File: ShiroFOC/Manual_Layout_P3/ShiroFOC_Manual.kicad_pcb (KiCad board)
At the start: 6 copper layers, 45 x 45 mm, 329 parts, among them J1 Motor phases - solder wires, J1001 TC2030-NL SWD, J101 DC input - solder wires, J201 USB-C service, J501 BRAKE RESISTOR, J502 5V PWM FAN, J601 EXT ENCODER / HALL, J801 CAN 1, J802 CAN 2, Q201 CSD17483F4, Q301 CSD17483F4, Q501 ISZ080N10NM6 100V, Q801 CSD17483F4, Q802 CSD87502Q2, SW301 RESET, U1 CSD88599Q5DC, U2 CSD88599Q5DC, U201 LMR36510FADDAR, U202 USBLC6-2SC6, U203 TPS2121RUXR, U204 TLV75533PDYDR, U205 MPM3620AGQV-Z, U3 CSD88599Q5DC, U4 STSPIN32G4, U501 UCC27517ADBVR, U502 TLV3012BIDCKR, U503 74AHCT1G125W5-7, U601 AS5047P-ATSM, U602 TMUX1574PW, U603 74LVC3G17, U604 TPS2553DBVR, U701 BMI323, U801 TCAN3413DRBR, U901 CP2102N-A02-GQFN20, Y301 24MHz 7pF

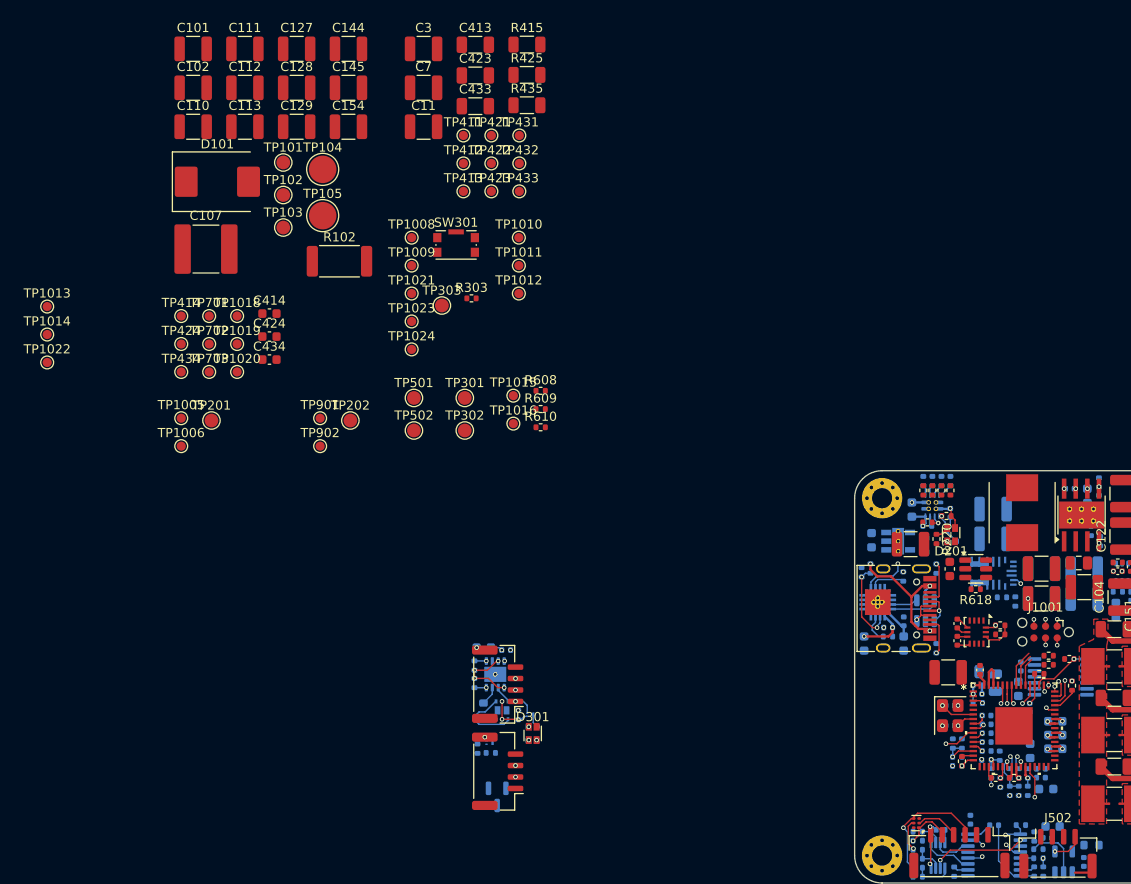
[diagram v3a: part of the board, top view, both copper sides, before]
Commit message: opamp circuits revised
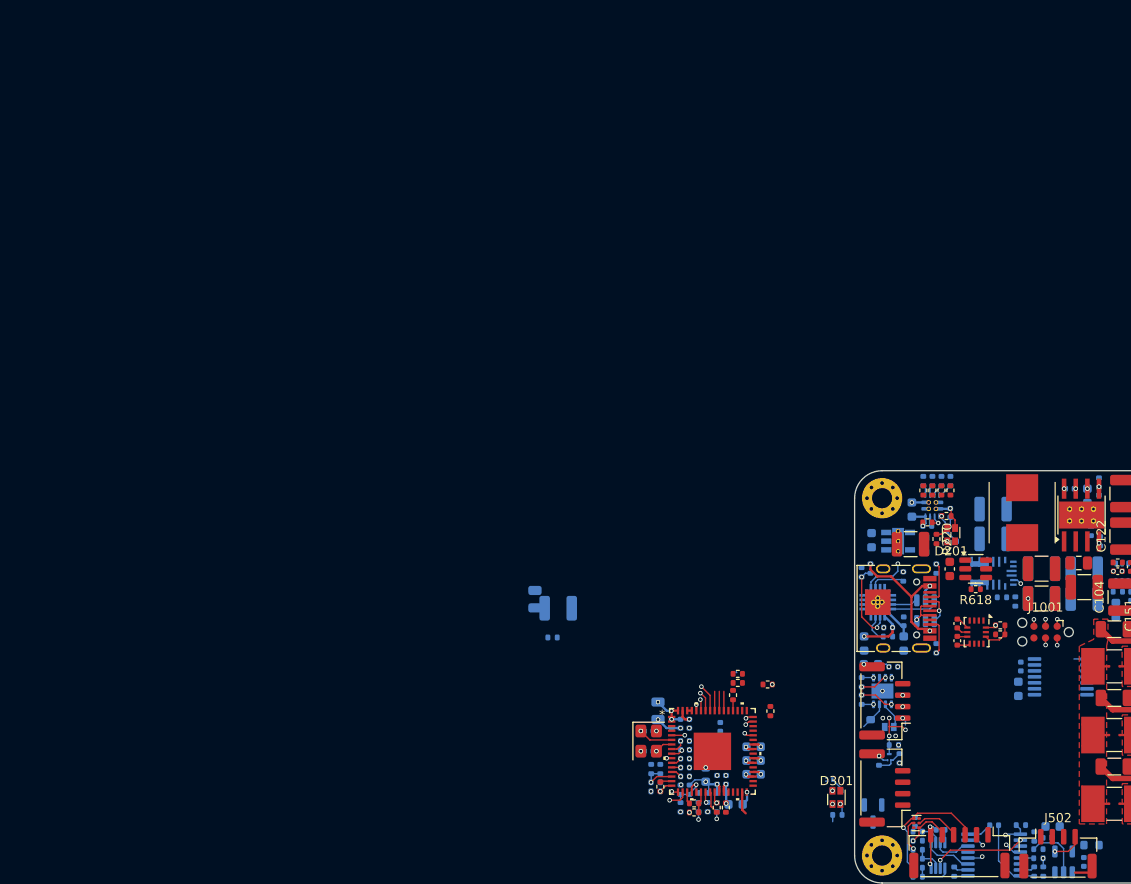
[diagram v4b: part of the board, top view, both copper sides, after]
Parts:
- removed C101, C102, C110, C111, C112, C113, C127, C128, C129, C144, C145, C154: 10uF, Capacitor_SMD:C_1210_3225Metric
- removed C107: RC DAMP C - TUNE, Capacitor_SMD:C_2220_5750Metric
- removed C11, C3, C7: 4.7uF, Capacitor_SMD:C_1210_3225Metric
- removed C413, C423, C433: TUNE DNP, Capacitor_SMD:C_1206_3216Metric
- removed C414, C424, C434: 47pF C0G, Capacitor_SMD:C_0603_1608Metric
- removed D101: VM TVS - SELECT AFTER TEST, Diode_SMD:D_SMC
- removed R102: RC DAMP R - TUNE, Resistor_SMD:R_2512_6332Metric
- removed R303: 2k2, Resistor_SMD:R_0402_1005Metric
- removed R415, R425, R435: TUNE DNP, Resistor_SMD:R_1206_3216Metric
- removed R608, R609, R610: 4.7k DNP, Resistor_SMD:R_0402_1005Metric
- removed SW301: RESET, Button_Switch_SMD:SW_Push_1P1T-SH_NO_CK_KMR2xxG
- removed TP1005: 5V_SYS, TestPoint:TestPoint_Pad_D1.0mm
- removed TP1006: 3V3, TestPoint:TestPoint_Pad_D1.0mm
- removed TP1008: SWDIO, TestPoint:TestPoint_Pad_D1.0mm
- removed TP1009: SWCLK, TestPoint:TestPoint_Pad_D1.0mm
- removed TP101: VM, TestPoint:TestPoint_Pad_D1.5mm
- removed TP1010: ENC_SPI_CLK, TestPoint:TestPoint_Pad_D1.0mm
- removed TP1011: SPI3_MISO, TestPoint:TestPoint_Pad_D1.0mm
- removed TP1012: ENC_SPI_MOSI, TestPoint:TestPoint_Pad_D1.0mm
- removed TP1013: FDCAN1_TX, TestPoint:TestPoint_Pad_D1.0mm
- removed TP1014: FDCAN1_RX, TestPoint:TestPoint_Pad_D1.0mm
- removed TP1015: FEEDBACK_A_H1, TestPoint:TestPoint_Pad_D1.0mm
- removed TP1016: FEEDBACK_B_H2, TestPoint:TestPoint_Pad_D1.0mm
- removed TP1018: OPO_U1, TestPoint:TestPoint_Pad_D1.0mm
- removed TP1019: OPO_V1, TestPoint:TestPoint_Pad_D1.0mm
- removed TP102: GND, TestPoint:TestPoint_Pad_D1.5mm
- removed TP1020: OPO_W1, TestPoint:TestPoint_Pad_D1.0mm
- removed TP1021: CAN_TERM_DISABLE, TestPoint:TestPoint_Pad_D1.0mm
- removed TP1022: CAN_STB, TestPoint:TestPoint_Pad_D1.0mm
- removed TP1023: EXT_POWER_FAULT_N, TestPoint:TestPoint_Pad_D1.0mm
- removed TP1024: I2C2_SDA, TestPoint:TestPoint_Pad_D1.0mm
- removed TP103: VBUS_SENSE, TestPoint:TestPoint_Pad_D1.5mm
- removed TP104: VM BULK, TestPoint:TestPoint_Pad_D3.0mm
- removed TP105: GND BULK, TestPoint:TestPoint_Pad_D3.0mm
- removed TP201: PWR_SOURCE_STATUS, TestPoint:TestPoint_Pad_D1.5mm
- removed TP202: 5V_USB, TestPoint:TestPoint_Pad_D1.5mm
- removed TP301: VCC, TestPoint:TestPoint_Pad_D1.5mm
- removed TP302: SCREF, TestPoint:TestPoint_Pad_D1.5mm
- removed TP303: NRST, TestPoint:TestPoint_Pad_D1.5mm
- removed TP411, TP421, TP431: GL, TestPoint:TestPoint_Pad_D1.0mm
- removed TP412, TP422, TP432: SOURCE, TestPoint:TestPoint_Pad_D1.0mm
- removed TP413, TP423, TP433: PHASE, TestPoint:TestPoint_Pad_D1.0mm
- removed TP414, TP424, TP434: SCOPE GND, TestPoint:TestPoint_Pad_D1.0mm
- removed TP501: BRAKE_GATE, TestPoint:TestPoint_Pad_D1.5mm
- removed TP502: BRAKE_SWITCH, TestPoint:TestPoint_Pad_D1.5mm
- removed TP701: NTC_PHASE_A, TestPoint:TestPoint_Pad_D1.0mm
- removed TP702: NTC_PHASE_B, TestPoint:TestPoint_Pad_D1.0mm
- removed TP703: NTC_PHASE_C, TestPoint:TestPoint_Pad_D1.0mm
- removed TP901: USB_UART_TX, TestPoint:TestPoint_Pad_D1.0mm
- removed TP902: USB_UART_RX, TestPoint:TestPoint_Pad_D1.0mm
- C312, C313: moved to B.Cu
- R301, R428: moved to F.Cu
- moved C311 51.1 mm to (-57.4, -8.48)
- moved R604 47.0 mm to (-55.5, -4.30)
- moved R803 44.6 mm to (-17.6, 8.89), turned to 90 degrees
- moved R804 43.8 mm to (-19.8, 9.14)
- moved Q801 43.6 mm to (-18.7, 8.76), turned to 90 degrees
- moved C312 43.1 mm to (-54.9, -7.49), turned to 0 degrees
- moved C801 42.3 mm to (-18.3, -1.10)
- moved C802 42.3 mm to (-20.7, -1.37)
- moved J801 42.3 mm to (-19.2, 2.62)
- moved J802 42.3 mm to (-19.2, 12.1)
- moved Q802 42.3 mm to (-18.7, 5.47)
- moved R801 42.3 mm to (-21.7, 2.50)
- moved R805 42.3 mm to (-21.7, 0.59)
- moved R802 42.3 mm to (-20.8, 5.50)
- moved U801 42.3 mm to (-19.5, 1.55)
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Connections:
- J801 pad 4: /CAN interface/CAN_SHIELD -> GND
- J802 pad 4: /CAN interface/CAN_SHIELD -> GND
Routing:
- net /MCU / clock / SWD/SWDIO: track 9.69 -> 1.69 mm, vias 2 -> 1
- net VREF+: track 0.55 -> 6.71 mm, vias 3 -> 2
- net CAN_TERM_DISABLE: track 0.00 -> 5.43 mm, vias 0 -> 2
- net AS5047P_CS_N: track 6.60 -> 1.42 mm
- net GND: track 62.8 -> 67.7 mm, vias 15 -> 27
- net Net-(Q802A-S1): track 7.38 -> 2.63 mm, vias 0 -> 2
- net /CAN interface/CANH_BUS: track 12.0 -> 7.40 mm, vias 2 -> 1
- net USB_UART_RX: track 10.6 -> 6.62 mm, vias 2 -> 1
- net /CAN interface/CANL_BUS: track 12.1 -> 8.27 mm, vias 2 -> 1
- net CAN_STB: track 4.84 -> 1.30 mm, vias 2 -> 1
- net /Current / temperature/OPP_W1: track 4.59 -> 1.16 mm
- net VM: track 57.4 -> 54.2 mm
- net Net-(Q801-G): track 0.00 -> 3.00 mm
- net FAN_PWM: track 3.48 -> 0.55 mm
- net USB_UART_TX: track 2.75 -> 0.00 mm
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
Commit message: weekend progress
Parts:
- added C101: 10uF, Capacitor_SMD:C_1210_3225Metric, F.Cu at (39.1, -26.7)
- added C102: 10uF, Capacitor_SMD:C_1210_3225Metric, F.Cu at (39.1, -22.4)
- added C11: 4.7uF, Capacitor_SMD:C_1210_3225Metric, F.Cu at (64.2, -18.2)
- added C110: 10uF, Capacitor_SMD:C_1210_3225Metric, F.Cu at (39.1, -18.2)
- added C111: 10uF, Capacitor_SMD:C_1210_3225Metric, F.Cu at (44.7, -26.7)
- added C112: 10uF, Capacitor_SMD:C_1210_3225Metric, F.Cu at (44.7, -22.4)
- added C113: 10uF, Capacitor_SMD:C_1210_3225Metric, F.Cu at (44.7, -18.2)
- added C127: 10uF, Capacitor_SMD:C_1210_3225Metric, F.Cu at (50.4, -26.7)
- added C128: 10uF, Capacitor_SMD:C_1210_3225Metric, F.Cu at (50.4, -22.4)
- added C129: 10uF, Capacitor_SMD:C_1210_3225Metric, F.Cu at (50.4, -18.2)
- added C144: 10uF, Capacitor_SMD:C_1210_3225Metric, F.Cu at (56.0, -26.7)
- added C145: 10uF, Capacitor_SMD:C_1210_3225Metric, F.Cu at (56.0, -22.4)
- added C154: 10uF, Capacitor_SMD:C_1210_3225Metric, F.Cu at (56.0, -18.2)
- added C3: 4.7uF, Capacitor_SMD:C_1210_3225Metric, F.Cu at (64.2, -26.7)
- added C7: 4.7uF, Capacitor_SMD:C_1210_3225Metric, F.Cu at (64.2, -22.4)
- added R303: 2k2, Resistor_SMD:R_0402_1005Metric, B.Cu at (-13.3, 3.29)
- C311, C601, C602, C607, R315: moved to F.Cu
- J1: footprint ShiroFOCLib:WireSolder_Phase_1x03_P6.35mm_D2.90mm_Pad4.10mm -> ShiroFOCLib:WireSolder_Phase_1x03_P6.35mm_D3.00mm_Pad5.00x4.10mm_4xD0.40mm
- J101: footprint ShiroFOCLib:WireSolder_DC_1x02_P6.35mm_D2.70mm_Pad4.10mm -> ShiroFOCLib:WireSolder_DC_1x02_P6.35mm_D3.00mm_Pad5.00x4.10mm_4xD0.40mm
- J601: footprint Connector_JST:JST_GH_BM06B-GHS-TBT_1x06-1MP_P1.25mm_Vertical -> Connector_JST:JST_GH_SM06B-GHS-TB_1x06-1MP_P1.25mm_Horizontal
- J801, J802: footprint Connector_JST:JST_GH_BM04B-GHS-TBT_1x04-1MP_P1.25mm_Vertical -> Connector_JST:JST_GH_SM03B-GHS-TB_1x03-1MP_P1.25mm_Horizontal
- R309, R903, TH701, TH702, TH703: moved to B.Cu
- moved C118 68.8 mm to (10.8, 28.7), turned to 180 degrees
- moved C119 63.3 mm to (15.4, 28.8)
- moved C312 50.5 mm to (-6.23, 6.09), turned to -90 degrees
- moved C311 48.9 mm to (-9.55, 1.54), turned to 180 degrees
- moved TH701 44.3 mm to (10.3, -0.64)
- moved TH703 44.3 mm to (10.3, 14.3)
- moved TH702 42.4 mm to (10.3, 6.85)
- moved R604 41.9 mm to (-14.2, 3.29), turned to -90 degrees
- moved R103 35.3 mm to (-26.6, -0.18)
- moved R105 34.9 mm to (-29.6, 0.02)
- moved C314 33.5 mm to (-3.70, 4.70)
- moved R106 32.8 mm to (-28.6, 0.02), turned to -90 degrees
- moved R903 32.7 mm to (0.91, 5.88), turned to 0 degrees
- moved R311 32.7 mm to (-2.58, 0.56), turned to 90 degrees
- moved C607 32.5 mm to (-9.28, -14.0)
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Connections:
- C711 pad 1: NTC_PHASE_A -> NTC_PHASE_B
- C712 pad 1: NTC_PHASE_B -> NTC_PHASE_A
- R701 pad 2: /Current / temperature/NTC_A_RAW -> /Current / temperature/NTC_B_RAW
- R702 pad 2: /Current / temperature/NTC_B_RAW -> /Current / temperature/NTC_A_RAW
- R711 pad 1: /Current / temperature/NTC_A_RAW -> /Current / temperature/NTC_B_RAW
- R711 pad 2: NTC_PHASE_A -> NTC_PHASE_B
- R712 pad 1: /Current / temperature/NTC_B_RAW -> /Current / temperature/NTC_A_RAW
- R712 pad 2: NTC_PHASE_B -> NTC_PHASE_A
- TH701 pad 1: /Current / temperature/NTC_A_RAW -> /Current / temperature/NTC_B_RAW
- TH702 pad 1: /Current / temperature/NTC_B_RAW -> /Current / temperature/NTC_A_RAW
- U4 pad 11: NTC_PHASE_B -> NTC_PHASE_A
- U4 pad 12: NTC_PHASE_A -> NTC_PHASE_B
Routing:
- net CAN_TERM_DISABLE: track 5.43 -> 23.4 mm
- net I2C2_SCL: track 0.00 -> 17.0 mm, vias 0 -> 2
- net /CAN interface/CANL_BUS: track 8.27 -> 24.4 mm
- net FDCAN1_RX: track 4.42 -> 18.3 mm
- net I2C2_SDA: track 2.17 -> 15.5 mm
- net 3V3: track 40.0 -> 28.7 mm, vias 11 -> 15
- net FDCAN1_TX: track 7.24 -> 18.2 mm
- net /MCU / clock / SWD/NRST: track 2.40 -> 12.5 mm
- net /CAN interface/CANH_BUS: track 7.40 -> 17.2 mm
- net CAN_STB: track 1.30 -> 9.92 mm, vias 1 -> 2
- net SPI3_SCK_MCU: track 2.10 -> 10.1 mm, vias 0 -> 1
- net SPI3_MISO: track 2.10 -> 9.19 mm, vias 0 -> 1
- net VBUS_SENSE: track 3.13 -> 9.49 mm
- net AS5047P_CS_N: track 1.42 -> 7.77 mm
- net SPI3_MOSI_MCU: track 2.10 -> 8.22 mm, vias 0 -> 1
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
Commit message: half bridge progress
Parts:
- J1: footprint ShiroFOCLib:WireSolder_Phase_1x03_P6.35mm_D3.00mm_Pad5.00x4.10mm_4xD0.40mm -> ShiroFOCLib:WireSolder_Phase_1x03_P6.85mm_D3.00mm_Pad5.00x4.10mm_4xD0.40mm
- J101: footprint ShiroFOCLib:WireSolder_DC_1x02_P6.35mm_D3.00mm_Pad5.00x4.10mm_4xD0.40mm -> ShiroFOCLib:WireSolder_DC_1x02_P6.85mm_D3.00mm_Pad5.00x4.10mm_4xD0.40mm
- moved R607 9.66 mm to (-21.9, 12.6)
- moved C603 9.66 mm to (-16.4, 3.21)
- moved C604 9.66 mm to (-16.6, 12.6)
- moved C605 9.66 mm to (-21.5, 8.72)
- moved D601 9.66 mm to (-16.6, 12.6)
- moved J601 9.66 mm to (-19.3, 5.67)
- moved R103 9.66 mm to (-17.0, -0.80)
- moved R105 9.66 mm to (-20.0, -0.60)
- moved R106 9.66 mm to (-19.0, -0.60)
- moved R305 9.66 mm to (-16.4, 1.32)
- moved R306 9.66 mm to (-17.5, 8.62)
- moved R307 9.66 mm to (-21.5, -0.14)
- moved R605 9.66 mm to (-20.9, 12.6)
- moved R606 9.66 mm to (-18.9, 12.6)
- moved R615 9.66 mm to (-19.9, 12.6)
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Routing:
- net VM: track 57.9 -> 5.94 mm
- net GHS3: track 0.00 -> 23.7 mm, vias 1 -> 2
- net HS_RETURN_W: track 3.23 -> 23.7 mm
- net GHS1: track 0.00 -> 20.3 mm, vias 1 -> 2
- net GHS2: track 0.00 -> 19.4 mm, vias 1 -> 2
- net HS_RETURN_U: track 3.16 -> 21.3 mm
- net HS_RETURN_V: track 3.23 -> 20.2 mm
- net GLS1: track 4.81 -> 20.5 mm, vias 1 -> 2
- net I2C2_SCL: track 17.0 -> 2.37 mm
- net GLS2: track 4.44 -> 18.2 mm, vias 1 -> 2
- net GND: track 72.9 -> 59.4 mm, vias 54 -> 55
- net GLS3: track 4.06 -> 15.3 mm, vias 1 -> 2
- net CAN_TERM_DISABLE: track 23.4 -> 14.1 mm
- net PHASE_U: track 4.78 -> 0.00 mm
- net /Three-phase bridge/LS_SOURCE_W: track 2.31 -> 0.00 mm
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- removed copper zone on F.Cu, net /Three-phase bridge/LS_SOURCE_U
- removed copper zone on F.Cu, net /Three-phase bridge/LS_SOURCE_V
- removed copper zone on F.Cu, net /Three-phase bridge/LS_SOURCE_W
- removed copper zone on F.Cu, net GND
- removed copper zone on F.Cu, net VM
